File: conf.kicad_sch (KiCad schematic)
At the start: 59 parts, among them M401 LG, M402 LG, M403 LG, Q401 DNLS350E, Q402 DNLS350E, Q403 DPLS350E, Q404 DPLS350E, U401 SN74LVC1G04DBVR, U402 4085, U403 AD567xR, U404 TLV9352, U405 4041

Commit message: add pcb layout for connection of adc circuit
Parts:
- M401, M402, M403: symbol pss:Lightguide_D4mm_L22.86mm_Dout5mm -> pss:Lightguide_D4mm_L4.78mm_Dout5mm
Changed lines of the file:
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@@
 		(title "Power Supply Sink")
 		(date "2024-12-11")
-		(rev "0.14.5")
+		(rev "0.14.6")
 		(company "Open Battery Tester")
 		(comment 1 "Configuration")
@@
 	)
 	(symbol
-		(lib_id "pss:Lightguide_D4mm_L22.86mm_Dout5mm")
+		(lib_id "pss:Lightguide_D4mm_L4.78mm_Dout5mm")
 		(at 165.1 149.86 0)
 		(unit 1)
@@
 	)
 	(symbol
-		(lib_id "pss:Lightguide_D4mm_L22.86mm_Dout5mm")
+		(lib_id "pss:Lightguide_D4mm_L4.78mm_Dout5mm")
 		(at 144.78 149.86 0)
 		(unit 1)
@@
 	)
 	(symbol
-		(lib_id "pss:Lightguide_D4mm_L22.86mm_Dout5mm")
+		(lib_id "pss:Lightguide_D4mm_L4.78mm_Dout5mm")
 		(at 154.94 149.86 0)
 		(unit 1)

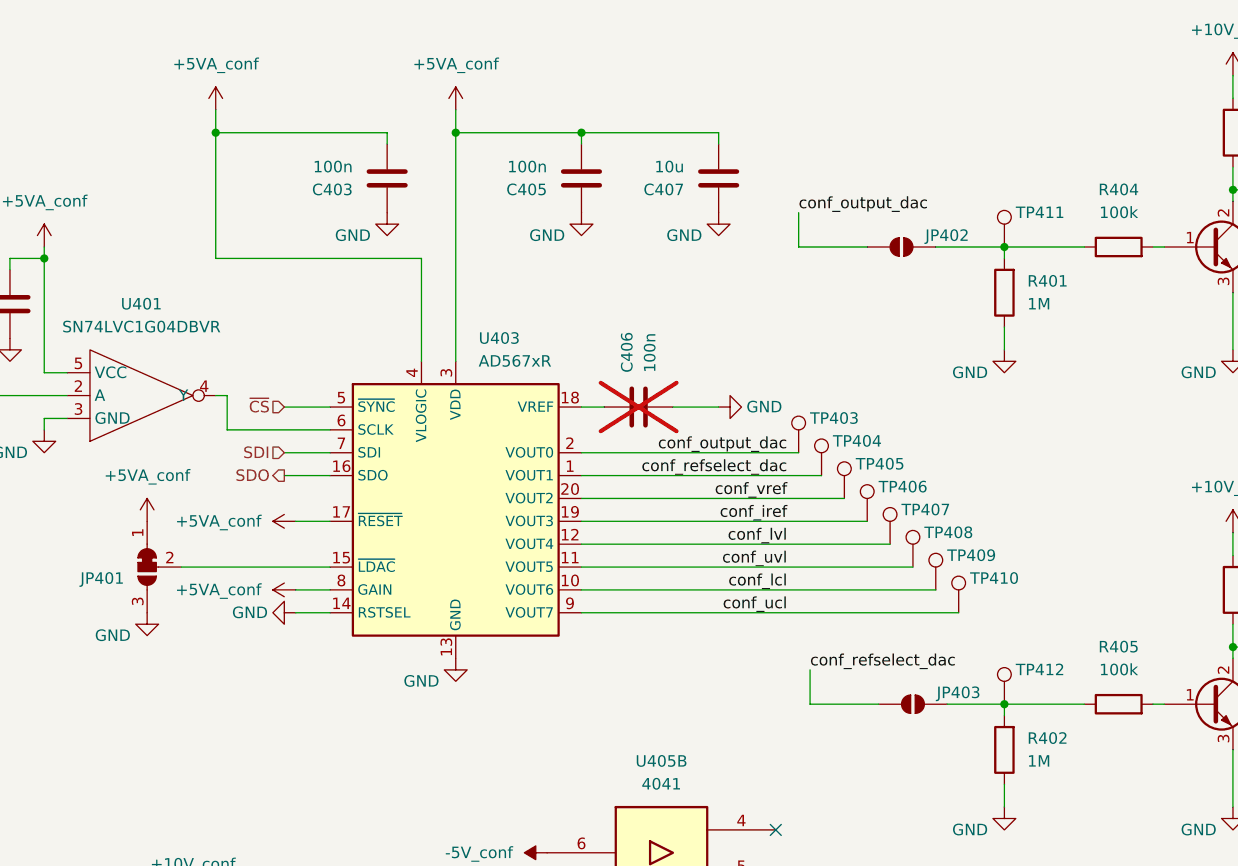
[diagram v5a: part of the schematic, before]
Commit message: add pcb layout for conf sub circuit - prototype
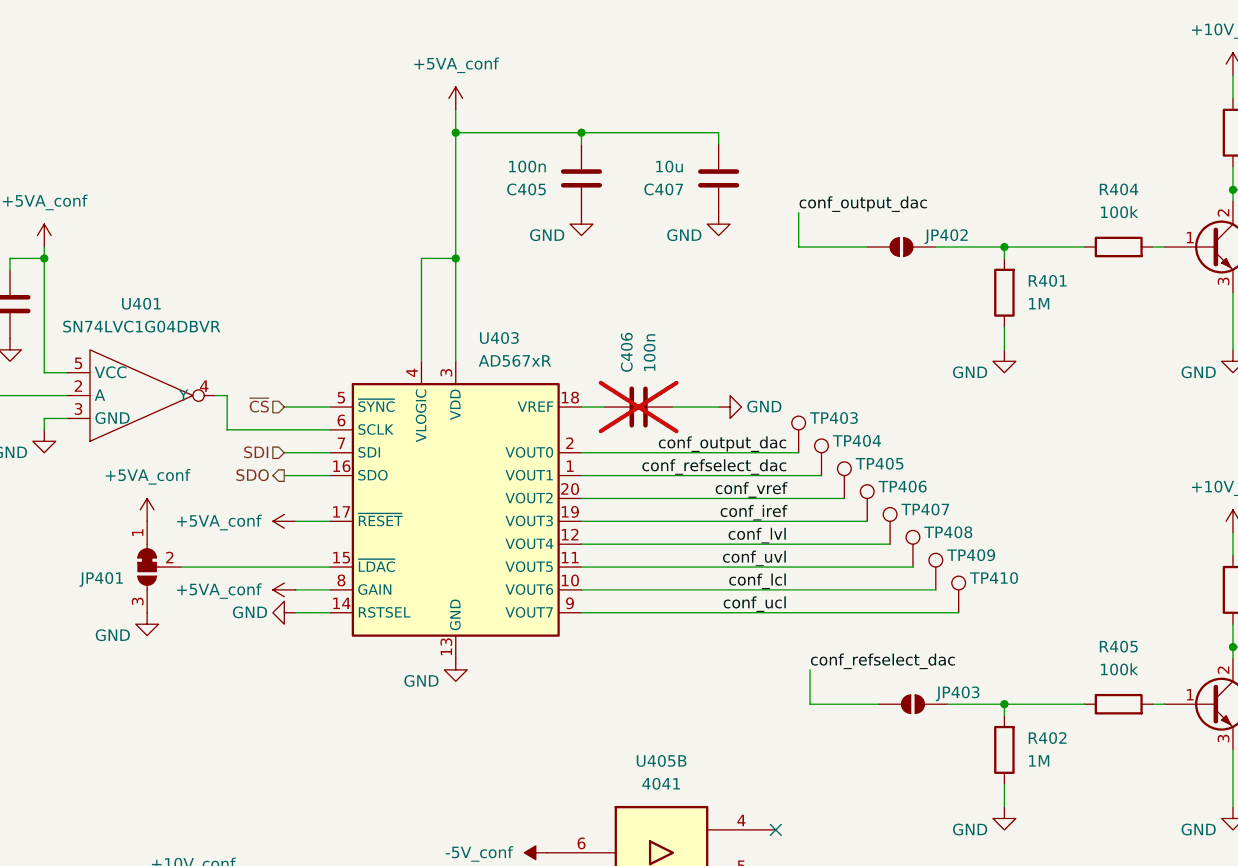
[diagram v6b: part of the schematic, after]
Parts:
- removed C403: 100n, pss:C_0805_2012Metric_Pad1.18x1.45mm_HandSolder, symbol pss:C
- removed TP411, TP412: ~, pss:TP_0805_2012Metric, symbol pss:TestPoint

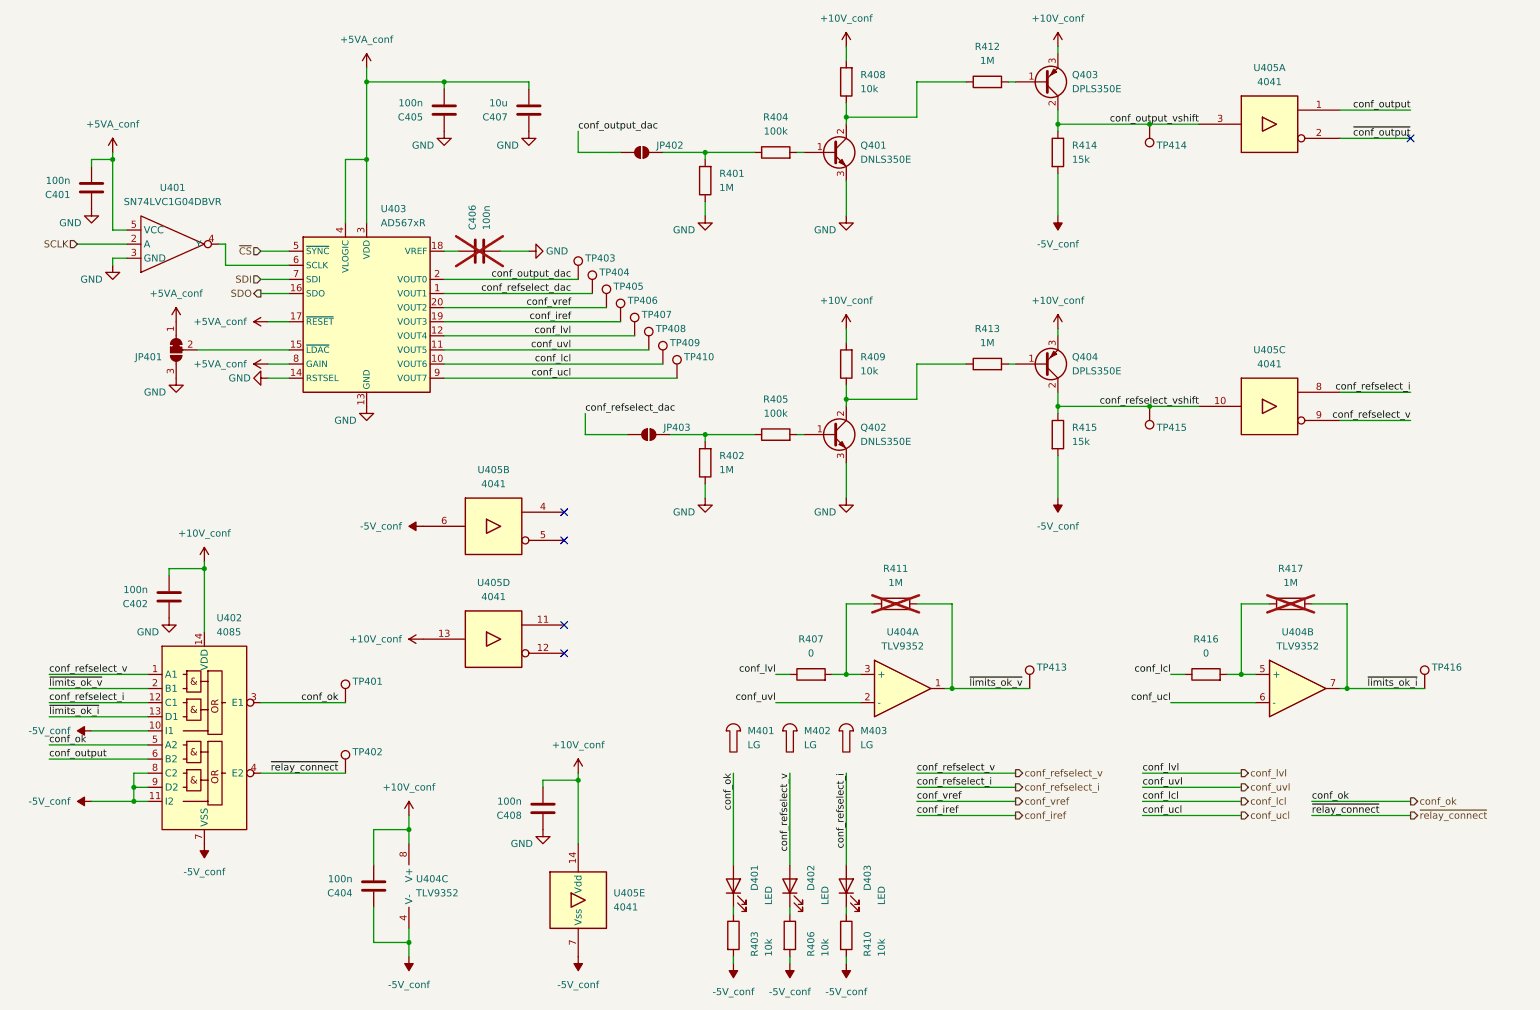
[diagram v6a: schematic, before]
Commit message: add pcb layout for conf sub circuit
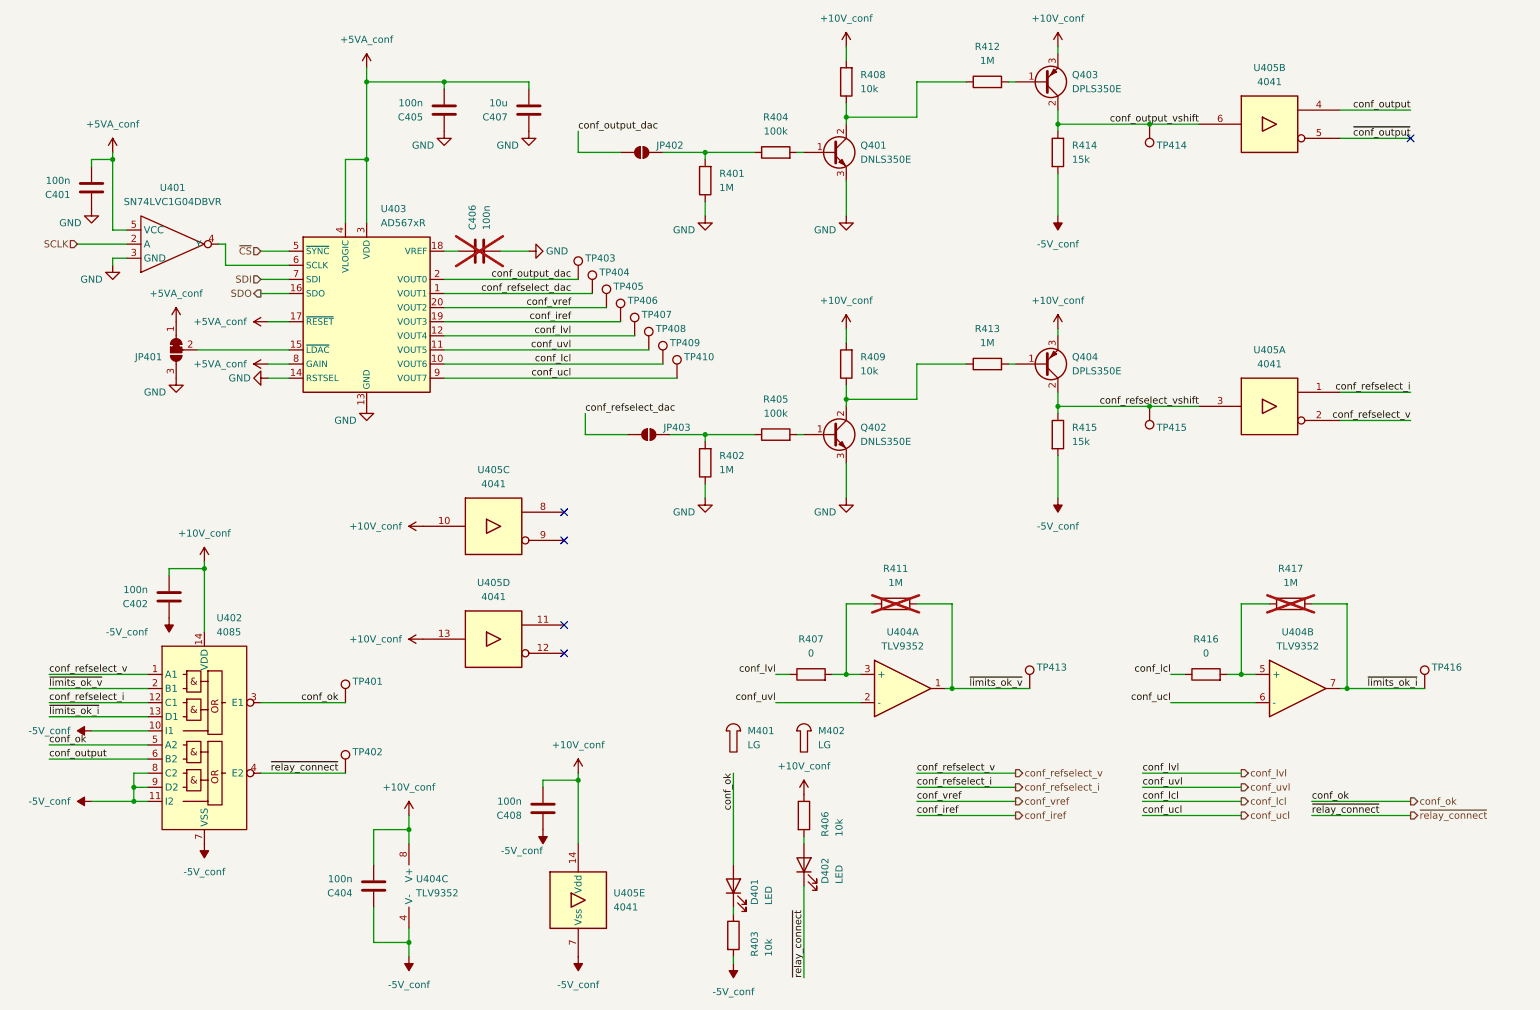
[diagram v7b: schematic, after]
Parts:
- removed D403: LED, pss:LED_0805_2012Metric_Pad1.15x1.40mm_HandSolder, symbol pss:LED
- removed M403: LG, symbol pss:Lightguide_D4mm_L4.78mm_Dout5mm
- removed R410: 10k, pss:R_1210_3225Metric_Pad1.30x2.65mm_HandSolder, symbol pss:R
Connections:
- net +10V_conf: now also R406.1, U405.10
- net -5V_conf: now also C402.1, C408.1; no longer R406.2, U405.6
- net GND: no longer C402.1, C408.1
- net conf_output: now also U405.4; no longer U405.1
- net conf_output_vshift: now also U405.6; no longer U405.3
- net conf_refselect_i: now also U405.1; no longer U405.8
- net conf_refselect_v: now also U405.2; no longer D402.2 (A), U405.9
- net conf_refselect_vshift: now also U405.3; no longer U405.10
- net ~{conf_output}: now also U405.5; no longer U405.2
- net ~{relay_connect}: now also D402.1 (K)
- new net: D402.2 (A), R406.2
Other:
- moved on the sheet: D402, M402, R406
